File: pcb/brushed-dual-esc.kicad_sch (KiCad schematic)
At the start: 2 parts, among them J3 Conn_ARM_JTAG_SWD_10, U3 STM32C011F4Ux

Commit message: Finish design
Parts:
- removed J3: Conn_ARM_JTAG_SWD_10, Connector_PinHeader_1.27mm:PinHeader_2x05_P1.27mm_Vertical, symbol Connector:Conn_ARM_JTAG_SWD_10
- added C1, C3, C8: 100n, Capacitor_SMD:C_0603_1608Metric, symbol Device:C_Small
- added C12, C13: 22u, Capacitor_SMD:C_0603_1608Metric, symbol Device:C_Small
- added C14, C15: 1u, Capacitor_SMD:C_0603_1608Metric, symbol Device:C_Small
- added C2, C4: 47u, Capacitor_SMD:C_1210_3225Metric, symbol Device:C_Small
- added C9: 4.7u, Capacitor_SMD:C_0603_1608Metric, symbol Device:C_Small
- added J1: XT30PW-M, Connector_AMASS:AMASS_XT30PW-M_1x02_P2.50mm_Horizontal, symbol Connector:Conn_01x02_Pin
- added J2: Conn_02x03_Odd_Even, Connector_PinHeader_2.54mm:PinHeader_2x03_P2.54mm_Horizontal, symbol Connector_Generic:Conn_02x03_Odd_Even
- added J3: TC2030-NL, Connector:Tag-Connect_TC2030-IDC-NL_2x03_P1.27mm_Vertical, symbol Connector:Conn_ARM_SWD_TagConnect_TC2030-NL
- added J6, J7: XT30PW-F, Connector_AMASS:AMASS_XT30PW-F_1x02_P2.50mm_Horizontal, symbol Connector:Conn_01x02_Socket
- added R1: 30k, Resistor_SMD:R_0603_1608Metric, symbol Device:R_Small_US
- added R2: 10k, Resistor_SMD:R_0603_1608Metric, symbol Device:R_Small_US
- added R3, R4: 750, Resistor_SMD:R_0603_1608Metric, symbol Device:R_Small_US
- added U2: AZ1117-5.0, Package_TO_SOT_SMD:SOT-223-3_TabPin2, symbol Regulator_Linear:AZ1117-5.0
- added U4, U6: DRV8231ADSGR, Package_SON:WSON-8-1EP_2x2mm_P0.5mm_EP0.9x1.6mm, symbol Driver_Motor_TI:DRV8231ADSGR
- added U5: TLV77133PDBVR, Package_TO_SOT_SMD:SOT-23-5, symbol Regulator_Linear_TI:TLV77133PDBVR
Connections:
- net +3V3: now also U3.2 (VDD), C15.1, C8.1, C9.1, J3.1 (VCC), U4.4 (VREF), U5.5 (OUT), U6.4 (VREF)
- net GND: now also C1.2, C12.2, C13.2, C14.2, C15.2, C2.2, C3.2, C4.2, C8.2, C9.2, J1.1 (Pin_1), J2.5 (Pin_5), J2.6 (Pin_6), J3.5 (GND), R2.2, R3.2, R4.2, U2.1 (GND), U4.7 (GND), U4.9 (PAD), U5.4 (GND), U6.7 (GND), U6.9 (PAD)
- net SWCLK: now also J3.4 (SWCLK)
- net SWDIO: now also J3.2 (SWDIO)
- net ~{RESET}: now also J3.3 (~{RESET})
- net DRV2_ISENSE: now reaches U3.12 (PA7)
- net DRV2_ISENSE: now also R4.1, U6.1 (IPROPI)
- net DRV2_IN2: now reaches U3.13 (PA8)
- net DRV2_IN2: now also U6.2 (IN2)
- net DRV2_IN1: now reaches U3.14 (PA9/PA11)
- net DRV2_IN1: now also U6.3 (IN1)
- net BATT_SENSE: now reaches U3.15 (PA10/PA12)
- net BATT_SENSE: now also R1.2, R2.1
- net RX_CH2: now reaches U3.18 (PB6)
- net RX_CH2: now also J2.1 (Pin_1)
- net RX_CH1: now reaches U3.19 (PB7)
- net RX_CH1: now also J2.2 (Pin_2)
- net DRV1_ISENSE: now reaches U3.5 (PA0)
- net DRV1_ISENSE: now also R3.1, U4.1 (IPROPI)
- net DRV1_IN1: now reaches U3.6 (PA1)
- net DRV1_IN1: now also U4.3 (IN1)
- net DRV1_IN2: now reaches U3.7 (PA2)
- net DRV1_IN2: now also U4.2 (IN2)
- new net +5V: C12.1, C14.1, J2.3 (Pin_3), J2.4 (Pin_4), U2.2 (VO), U5.1 (IN), U5.3 (EN)
- new net +BATT: C1.1, C13.1, C2.1, C3.1, C4.1, J1.2 (Pin_2), R1.1, U2.3 (VI), U4.5 (VM), U6.5 (VM)
- new net DRV1_OUT1: J6.2 (Pin_2), U4.6 (OUT1)
- new net DRV1_OUT2: J6.1 (Pin_1), U4.8 (OUT2)
- new net DRV2_OUT1: J7.2 (Pin_2), U6.6 (OUT1)
- new net DRV2_OUT2: J7.1 (Pin_1), U6.8 (OUT2)
- no-connect marks 2 -> 7
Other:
- removed sheet Motor Driver
- removed sheet Motor Driver1
- note added: "1500uA/A"
- note added: "3.3V LDO"
- note added: "3S LiPo 11.1V what's the max input voltage?"
- note added: "5V LDO as BEC"
- note added: "Battery connection"
- note added: "Debug"
- note added: "MCU STM32C011"
- note added: "Motor Driver 1"
- note added: "Motor Driver 2"
- note added: "Reciever"

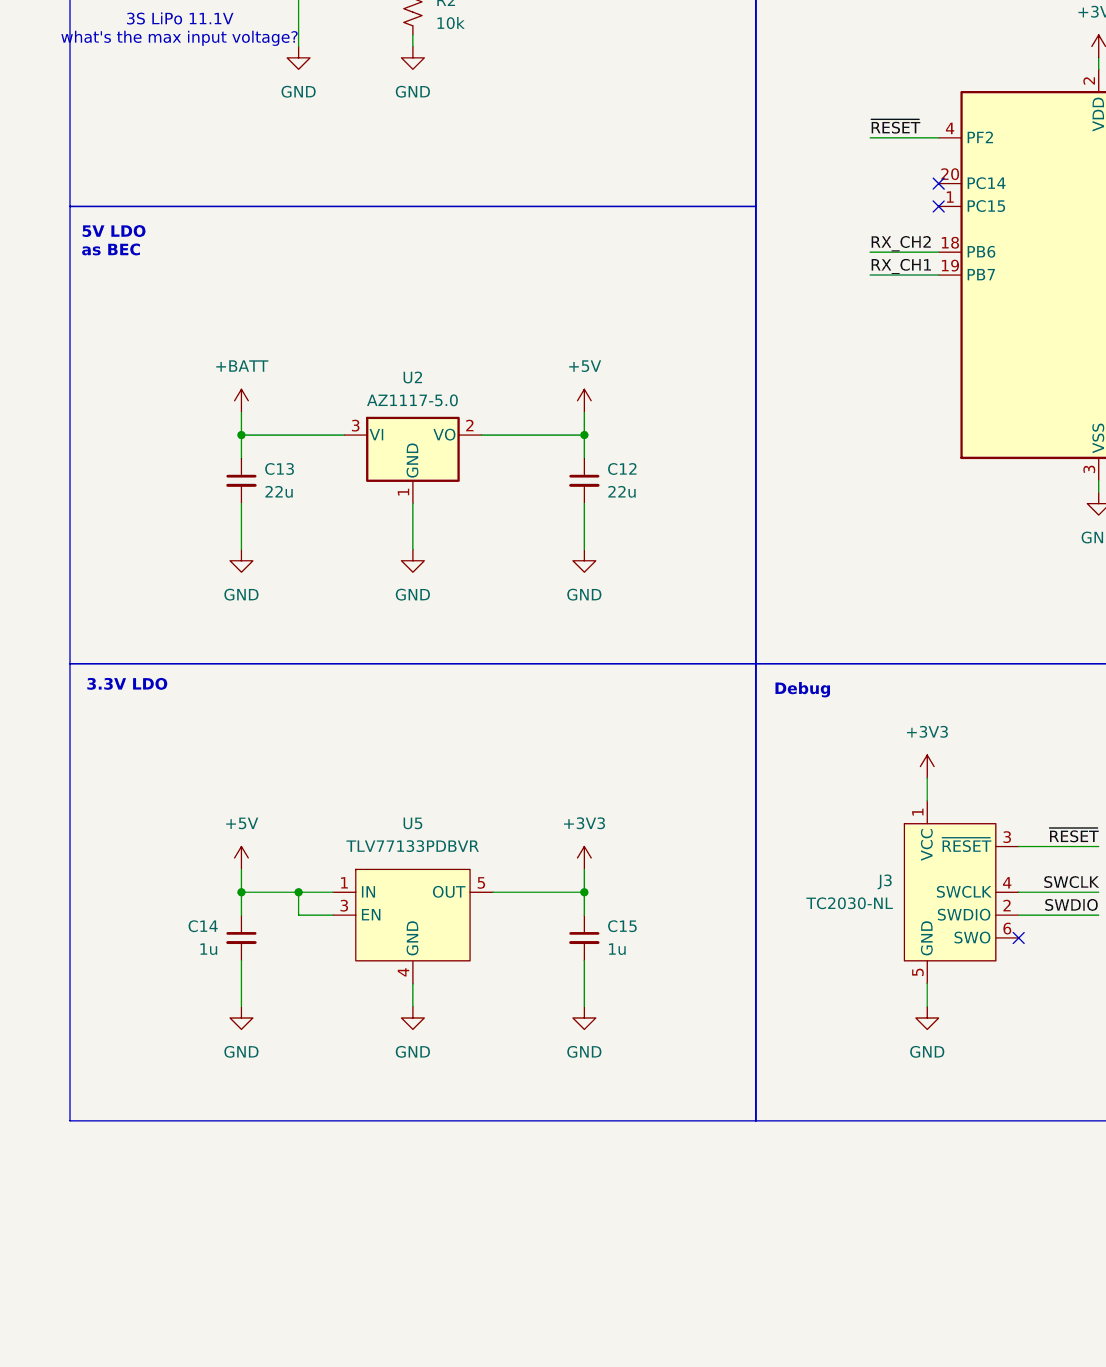
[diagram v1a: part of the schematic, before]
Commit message: Add status LED on spare pin
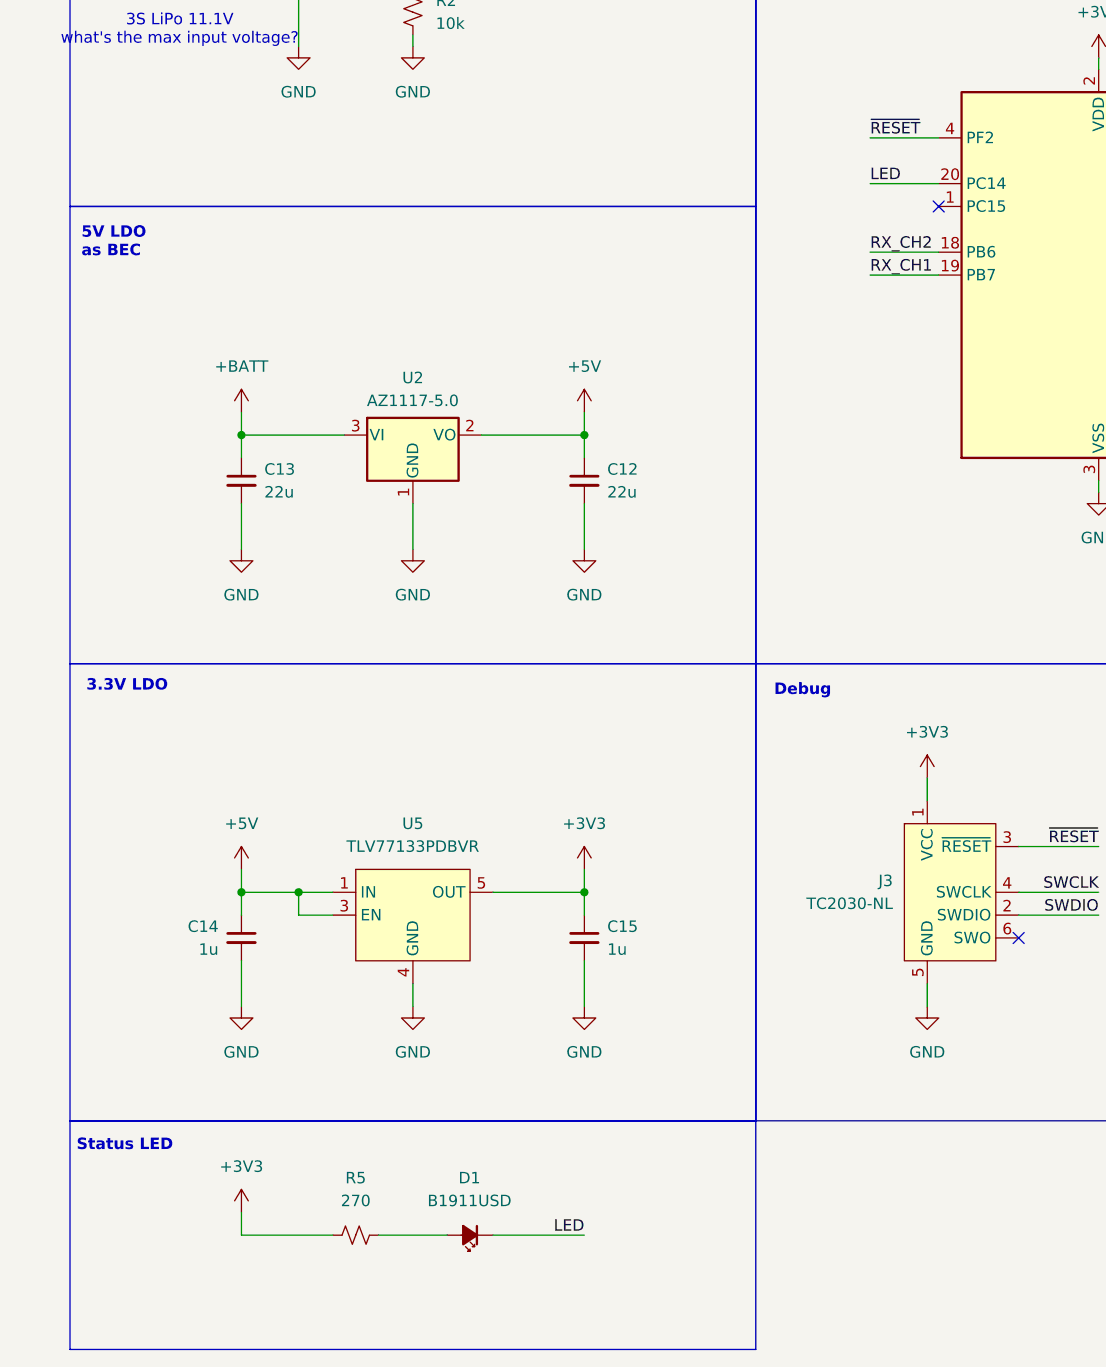
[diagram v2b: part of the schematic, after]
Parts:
- added D1: B1911USD, LED_SMD:LED_0603_1608Metric, symbol Device:LED_Small_Filled
- added R5: 270, Resistor_SMD:R_0603_1608Metric, symbol Device:R_Small_US
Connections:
- net +3V3: now also R5.1
- net LED: now reaches U3.20 (PC14)
- net LED: now also D1.1 (K)
- new net: D1.2 (A), R5.2
- no-connect marks 7 -> 6
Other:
- note added: "Status LED"

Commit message: Fix capacitor siutation
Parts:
- removed C2, C4: 47u, Capacitor_SMD:C_1210_3225Metric, symbol Device:C_Small
- removed C3: 100n, Capacitor_SMD:C_0603_1608Metric, symbol Device:C_Small
- added C10, C11, C12, C13, C16, C17: UMK107BJ105KA-T, Capacitor_SMD:C_0603_1608Metric, symbol Device:C_Small
- added C2: ESS107M016AC2KA, Capacitor_THT:CP_Radial_D5.0mm_P2.00mm, symbol Device:C_Polarized_Small_US
- C1: renamed from C13; value 22u -> 22u 16V
- C14, C15: value 1u -> UMK107BJ105KA-T
- C3: renamed from C12; value 22u -> 22u 16V
- C7: renamed from C1; value 100n -> UMK107BJ105KA-T
- C8: value 100n -> UMK107BJ105KA-T
- C9: value 4.7u -> UMK107BJ105KA-T
- renumbered J3 to J2, J2 to J3, J6 to J4, J7 to J5, R5 to R1, R1 to R2, R2 to R3, R3 to R4, R4 to R5, U2 to U1, U5 to U2, U6 to U5
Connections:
- net +3V3: now also C13.1, C16.1, C17.1; no longer C8.1, C9.1
- net +BATT: now also C8.1, C9.1, C10.1, C11.1, C12.1, C2.1
- net GND: now also C10.2, C11.2, C12.2, C13.2, C16.2, C17.2, C2.2
- net LED: now also U3.1 (PC15); no longer U3.20 (PC14)
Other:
- note added: "100u 16V"
- note added: "1u 50V"
- note added: "3S LiPo 11.1V max 18V"
- note added: "Motor driver Bulk decoupling"
- note removed: "3S LiPo 11.1V what's the max input voltage?"

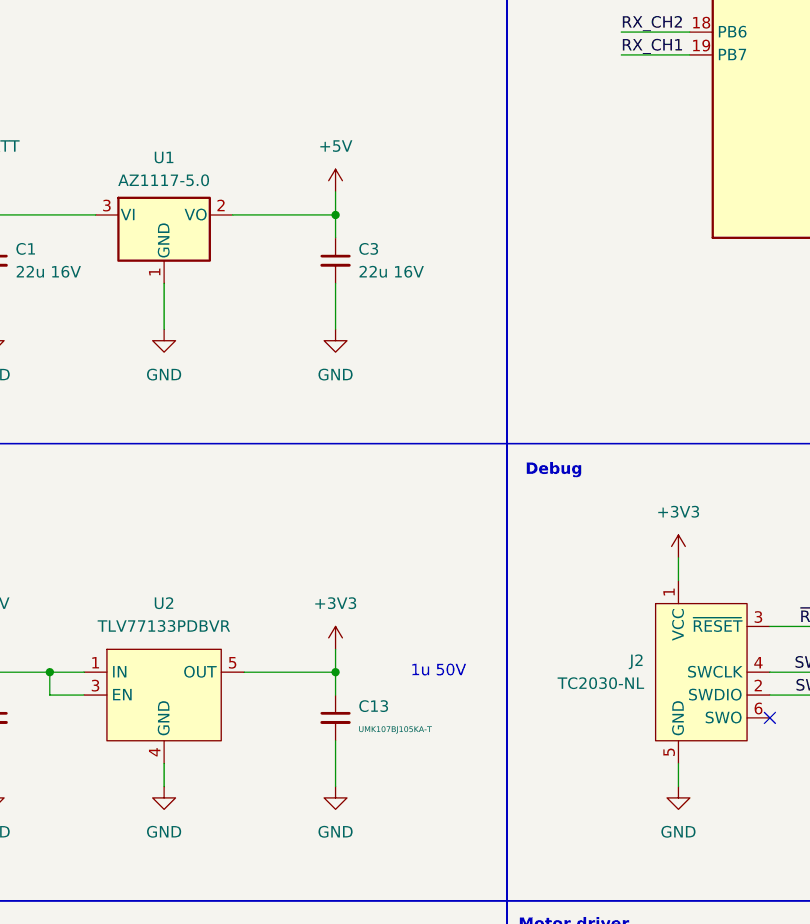
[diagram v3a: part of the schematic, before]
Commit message: Add testpoints and imrpove silkscreen
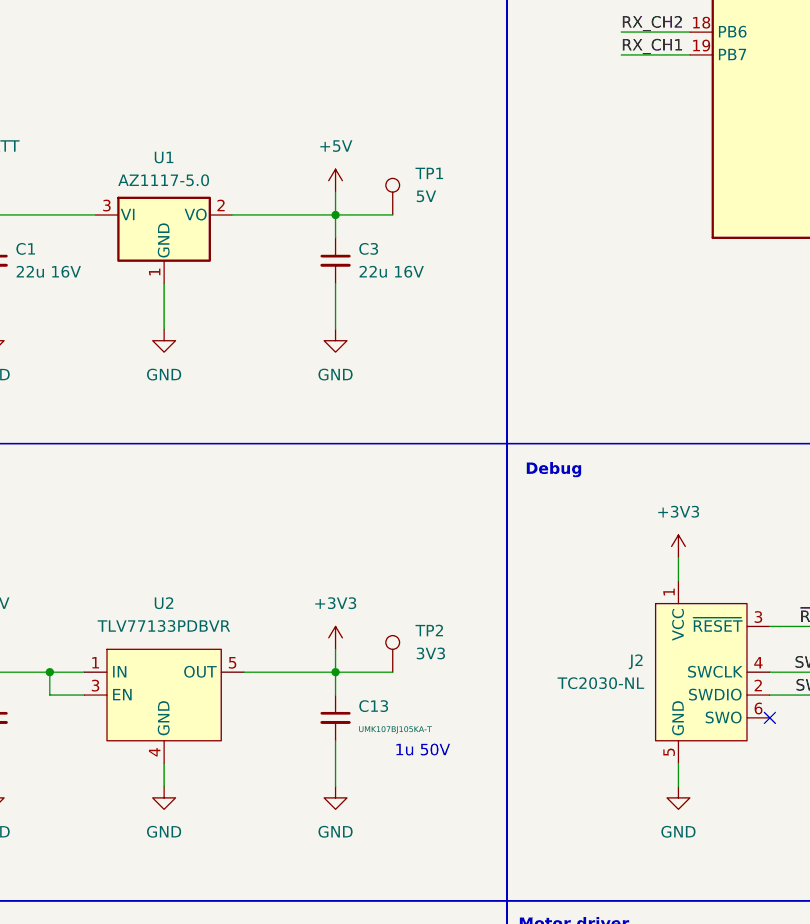
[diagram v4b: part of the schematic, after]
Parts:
- added TP1: 5V, TestPoint:TestPoint_Pad_D2.0mm, symbol Connector:TestPoint
- added TP2: 3V3, TestPoint:TestPoint_Pad_D1.5mm, symbol Connector:TestPoint
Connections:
- net +3V3: now also TP2.1
- net +5V: now also TP1.1
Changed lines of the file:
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@@
 	(text "1u 50V"
 		(exclude_from_sim no)
-		(at 81.28 139.7 0)
+		(at 79.502 148.59 0)
 		(effects
 			(font
@@
 	(wire
 		(pts
+			(xy 69.85 88.9) (xy 76.2 88.9)
+		)
+		(stroke
+			(width 0)
+			(type default)
+		)
+	)
+	(wire
+		(pts
 			(xy 224.79 119.38) (xy 224.79 121.92)
 		)
@@
 	(wire
 		(pts
+			(xy 69.85 139.7) (xy 76.2 139.7)
+		)
+		(stroke
+			(width 0)
+			(type default)
+		)
+	)
+	(wire
+		(pts
 			(xy 139.7 29.21) (xy 139.7 27.94)
 		)
@@
 	)
 	(symbol
+		(lib_id "Connector:TestPoint")
+		(at 76.2 88.9 0)
+		(unit 1)
+		(exclude_from_sim no)
+		(in_bom yes)
+		(on_board yes)
+		(dnp no)
+		(fields_autoplaced yes)
+		(property "Reference" "TP1"
+			(at 78.74 84.3279 0)
+			(effects
+				(font
+					(size 1.27 1.27)
+				)
+				(justify left)
+			)
+		)
+		(property "Value" "5V"
+			(at 78.74 86.8679 0)
+			(effects
+				(font
+					(size 1.27 1.27)
+				)
+				(justify left)
+			)
+		)
+		(property "Footprint" "TestPoint:TestPoint_Pad_D2.0mm"
+			(at 81.28 88.9 0)
+			(effects
+				(font
+					(size 1.27 1.27)
+				)
+				(hide yes)
+			)
+		)
+		(property "Datasheet" "~"
+			(at 81.28 88.9 0)
+			(effects
+				(font
+					(size 1.27 1.27)
+				)
+				(hide yes)
+			)
+		)
+		(property "Description" "test point"
+			(at 76.2 88.9 0)
+			(effects
+				(font
+					(size 1.27 1.27)
+				)
+				(hide yes)
+			)
+		)
+		(pin "1"
+		)
+		(instances
+			(project ""
+				(path "/624d6987-cb00-44c1-bd75-457d49fec660"
+					(reference "TP1")
+					(unit 1)
+				)
+			)
+		)
+	)
+	(symbol
 		(lib_id "MCU_ST_STM32C0:STM32C011F4Ux")
 		(at 127 71.12 0)
@@
 					(unit 1)
 				)
+			)
+		)
+	)
+	(symbol
+		(lib_id "Connector:TestPoint")
+		(at 76.2 139.7 0)
+		(unit 1)
+		(exclude_from_sim no)
+		(in_bom yes)
+		(on_board yes)
+		(dnp no)
+		(fields_autoplaced yes)
+		(property "Reference" "TP2"
+			(at 78.74 135.1279 0)
+			(effects
+				(font
+					(size 1.27 1.27)
+				)
+				(justify left)
+			)
+		)
+		(property "Value" "3V3"
+			(at 78.74 137.6679 0)
+			(effects
+				(font
+					(size 1.27 1.27)
+				)
+				(justify left)
+			)
+		)
+		(property "Footprint" "TestPoint:TestPoint_Pad_D1.5mm"
+			(at 81.28 139.7 0)
+			(effects
+				(font
+					(size 1.27 1.27)
+				)
+				(hide yes)
+			)
+		)
+		(property "Datasheet" "~"
+			(at 81.28 139.7 0)
+			(effects
+				(font
+					(size 1.27 1.27)
+				)
+				(hide yes)
+			)
+		)
+		(property "Description" "test point"
+			(at 76.2 139.7 0)
+			(effects
+				(font
+					(size 1.27 1.27)
+				)
+				(hide yes)
+			)
+		)
+		(pin "1"
+		)
+		(instances
+			(project "brushed-dual-esc"
+				(path "/624d6987-cb00-44c1-bd75-457d49fec660"
+					(reference "TP2")
+					(unit 1)
+				)

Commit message: Add step file
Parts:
- removed C11, C8: UMK107BJ105KA-T, Capacitor_SMD:C_0603_1608Metric, symbol Device:C_Small
- C1, C3: footprint Capacitor_SMD:C_0603_1608Metric -> Capacitor_SMD:C_0805_2012Metric
- R2: value 30k -> 47k
- renumbered C9 to C11, C14 to C2, C13 to C4, C2 to C5, C15 to C6, C16 to C7, C17 to C8, C7 to C9
